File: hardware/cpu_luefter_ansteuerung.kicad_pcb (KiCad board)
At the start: 2 copper layers, 26 parts, among them IC1 ATMEGA8A-A, P1 POWER 12V DC, P2 ISP, P3 CPU LUEFTER, Q1 BC817-40, SW1 SW_PUSH, U1 7805, U2 CD4543, Y1 Crystal 12MHz

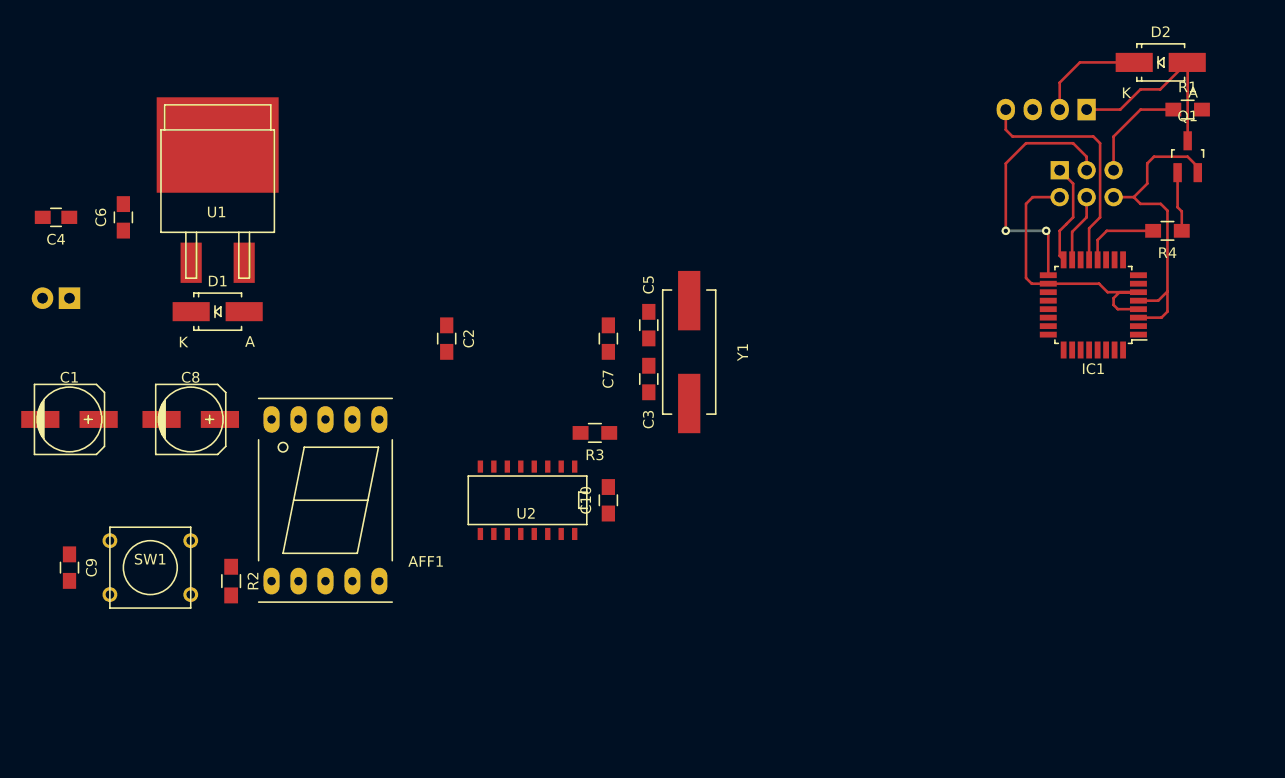
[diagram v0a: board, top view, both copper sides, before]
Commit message: Portierung zu KiCad 5.1.2
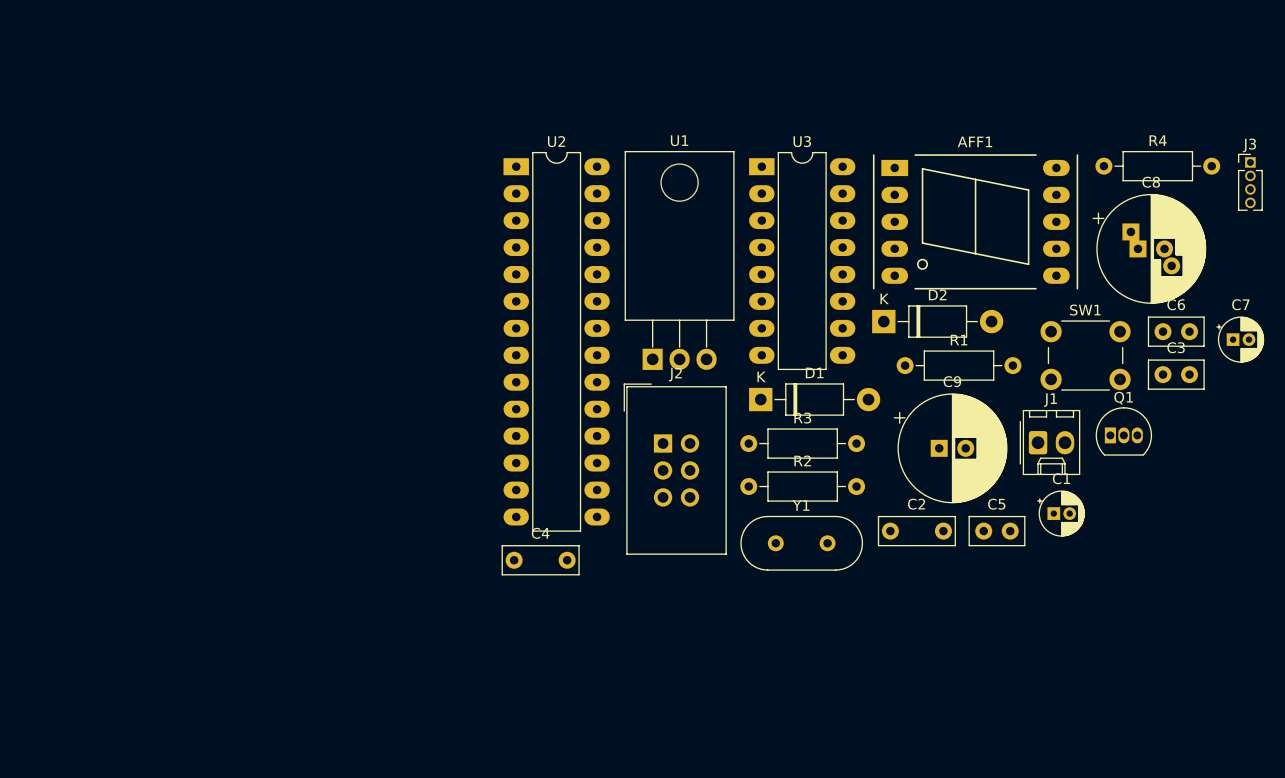
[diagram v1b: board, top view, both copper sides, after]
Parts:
- removed C10: 100n, Capacitors_SMD:C_0805_HandSoldering
- removed IC1: ATMEGA8A-A, Housings_QFP:TQFP-32_7x7mm_Pitch0.8mm
- removed P1: POWER 12V DC, Pin_Headers:Pin_Header_Straight_1x02
- removed P2: ISP, Pin_Headers:Pin_Header_Straight_2x03
- removed P3: CPU LUEFTER, Pin_Headers:Pin_Header_Straight_1x04
- added J1: Power 12V DC, Connector_Molex:Molex_KK-254_AE-6410-02A_1x02_P2.54mm_Vertical, F.Cu at (172.6, 110.1)
- added J2: ISP, Connector_IDC:IDC-Header_2x03_P2.54mm_Vertical, F.Cu at (137.2, 110.2)
- added J3: CPU Lüfter, Connector_PinHeader_1.27mm:PinHeader_1x04_P1.27mm_Vertical, F.Cu at (192.6, 83.7)
- added U3: 4543, Package_DIP:DIP-16_W7.62mm_LongPads, F.Cu at (146.5, 84.1)
- AFF1: value 7SEGMENTS LTS-5811R -> 7SEGMENTS; footprint Displays_7-Segment:7SegmentLED_LTS6760_LTS6780 -> Display_7Segment:7SegmentLED_LTS6760_LTS6780
- C1: footprint Capacitors_SMD:c_elec_6.3x5.7 -> Capacitor_THT:CP_Radial_D4.0mm_P1.50mm
- C2, C4: value 100n -> 22p; footprint Capacitors_SMD:C_0805_HandSoldering -> Capacitor_THT:C_Disc_D7.0mm_W2.5mm_P5.00mm
- C3, C5: value 22p -> 100n; footprint Capacitors_SMD:C_0805_HandSoldering -> Capacitor_THT:C_Disc_D5.0mm_W2.5mm_P2.50mm
- C6: footprint Capacitors_SMD:C_0805_HandSoldering -> Capacitor_THT:C_Disc_D5.0mm_W2.5mm_P2.50mm
- C7: value 100n -> 100u; footprint Capacitors_SMD:C_0805_HandSoldering -> Capacitor_THT:CP_Radial_D4.0mm_P1.50mm
- C8: value 100u -> 1u; footprint Capacitors_SMD:c_elec_6.3x5.7 -> Capacitor_THT:CP_Radial_D10.0mm_P2.50mm_P5.00mm
- C9: value 1u -> 100n; footprint Capacitors_SMD:C_0805_HandSoldering -> Capacitor_THT:CP_Radial_D10.0mm_P2.50mm
- D1, D2: footprint Diodes_SMD:SMA_Handsoldering -> Diode_THT:D_DO-41_SOD81_P10.16mm_Horizontal
- Q1: value BC817-40 -> BC337; footprint TO_SOT_Packages_SMD:SOT-23_Handsoldering -> Package_TO_SOT_THT:TO-92_Inline
- R1, R2, R3, R4: footprint Resistors_SMD:R_0805_HandSoldering -> Resistor_THT:R_Axial_DIN0207_L6.3mm_D2.5mm_P10.16mm_Horizontal
- SW1: value SW_PUSH -> SW_Push; footprint Buttons_Switches_ThroughHole:SW_PUSH_SMALL -> Button_Switch_THT:SW_PUSH_6mm_H5mm
- U1: footprint TO_SOT_Packages_SMD:SOT-404 -> Package_TO_SOT_THT:TO-220-3_Horizontal_TabDown
- U2: value CD4543 -> ATmega8-16PU; footprint SMD_Packages:SO-16-N -> Package_DIP:DIP-28_W7.62mm_LongPads
- Y1: footprint Crystals:Crystal_HC49-SD_SMD -> Crystal:Crystal_HC49-4H_Vertical
- moved C6 98.6 mm to (184.4, 99.7), turned to 0 degrees
- moved C1 93.2 mm to (174.1, 116.8)
- moved C8 90.7 mm to (182.0, 91.9)
- moved SW1 87.8 mm to (173.8, 99.7)
- moved C9 82.8 mm to (163.3, 110.7), turned to 0 degrees
- moved AFF1 62.1 mm to (159.1, 84.2), turned to 0 degrees
- moved C7 58.9 mm to (191.0, 100.4), turned to 0 degrees
- moved C4 53.9 mm to (123.2, 121.2), turned to 0 degrees
- moved D1 51.9 mm to (146.4, 106.1)
- moved R2 49.6 mm to (145.3, 114.3), turned to 0 degrees
- moved C3 48.5 mm to (184.4, 103.7), turned to 0 degrees
- moved C2 45.6 mm to (158.7, 118.5), turned to 0 degrees
- moved U1 43.5 mm to (136.3, 102.3)
- moved C5 37.1 mm to (167.5, 118.5), turned to 0 degrees
- moved R1 35.9 mm to (160.1, 102.9)
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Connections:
- AFF1 pad 1: Net-(AFF1-Pad1) -> +5V
- AFF1 pad 5: +5V -> Net-(AFF1-Pad5)
- C2 pad 1: +5V -> GND
- C2 pad 2: GND -> Net-(C2-Pad2)
- C3 pad 1: Net-(C3-Pad1) -> +12V
- C4 pad 1: +12V -> GND
- C4 pad 2: GND -> Net-(C4-Pad2)
- C5 pad 1: Net-(C5-Pad1) -> +5V
- C8 pad 1: +5V -> Net-(C8-Pad1)
- C9 pad 1: GND -> +5V
- C9 pad 2: Net-(C9-Pad2) -> GND
- Q1 pad 1: Net-(Q1-Pad1) -> Net-(D2-Pad2)
- Q1 pad 2: GND -> Net-(Q1-Pad2)
- Q1 pad 3: Net-(D2-Pad2) -> GND
- R1 pad 1: Net-(IC1-Pad29) -> Net-(J2-Pad5)
- R2 pad 1: +5V -> Net-(C8-Pad1)
- R2 pad 2: Net-(C9-Pad2) -> +5V
- R3 pad 1: +5V -> Net-(R3-Pad1)
- R3 pad 2: Net-(R3-Pad2) -> +5V
- R4 pad 1: Net-(Q1-Pad1) -> Net-(Q1-Pad2)
- R4 pad 2: Net-(IC1-Pad12) -> Net-(R4-Pad2)
- SW1 pad 1: Net-(C9-Pad2) -> Net-(C8-Pad1)
- U1 pad 1: +12V -> +5V
- U1 pad 3: +5V -> +12V
- U2 pad 1: Net-(R3-Pad2) -> Net-(J2-Pad5)
- U2 pad 10: Net-(AFF1-Pad7) -> Net-(C4-Pad2)
- U2 pad 11: Net-(AFF1-Pad3) -> Net-(U2-Pad11)
- U2 pad 12: Net-(AFF1-Pad2) -> Net-(U2-Pad12)
- U2 pad 13: Net-(AFF1-Pad1) -> Net-(U2-Pad13)
- U2 pad 14: Net-(AFF1-Pad9) -> Net-(R4-Pad2)
- U2 pad 15: Net-(AFF1-Pad10) -> Net-(J3-Pad4)
- U2 pad 16: +5V -> Net-(U2-Pad16)
- U2 pad 6: Net-(R3-Pad2) -> Net-(U2-Pad6)
- U2 pad 7: GND -> +5V
- U2 pad 9: Net-(AFF1-Pad8) -> Net-(C2-Pad2)
- Y1 pad 1: Net-(C5-Pad1) -> Net-(C2-Pad2)
- Y1 pad 2: Net-(C3-Pad1) -> Net-(C4-Pad2)
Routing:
- net GND: track 30.9 -> 0.00 mm
- net +5V: track 27.3 -> 0.00 mm
- net Net-(IC1-Pad17): track 24.6 -> 0.00 mm, vias 2 -> 0
- net Net-(IC1-Pad13): track 22.7 -> 0.00 mm
- net Net-(D2-Pad2): track 18.7 -> 0.00 mm
- net +12V: track 10.4 -> 0.00 mm
- net Net-(IC1-Pad29): track 9.86 -> 0.00 mm
- net Net-(IC1-Pad16): track 9.66 -> 0.00 mm
- net Net-(IC1-Pad12): track 7.46 -> 0.00 mm
- net Net-(IC1-Pad15): track 7.11 -> 0.00 mm
- net Net-(Q1-Pad1): track 5.65 -> 0.00 mm

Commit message: pcb angefangen, Bauteile schon mal angeordnet.
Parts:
- removed AFF1: 7SEGMENTS, Display_7Segment:7SegmentLED_LTS6760_LTS6780
- removed C5, C6: 100n, Capacitor_THT:C_Disc_D5.0mm_W2.5mm_P2.50mm
- removed C7: 100u, Capacitor_THT:CP_Radial_D4.0mm_P1.50mm
- removed C8: 1u, Capacitor_THT:CP_Radial_D10.0mm_P2.50mm_P5.00mm
- removed C9: 100n, Capacitor_THT:CP_Radial_D10.0mm_P2.50mm
- removed D2: 1N4001, Diode_THT:D_DO-41_SOD81_P10.16mm_Horizontal
- removed R1: 10k, Resistor_THT:R_Axial_DIN0207_L6.3mm_D2.5mm_P10.16mm_Horizontal
- removed Y1: Crystal 12MHz, Crystal:Crystal_HC49-4H_Vertical
- added R10: 560, Resistor_THT:R_Axial_DIN0207_L6.3mm_D2.5mm_P10.16mm_Horizontal, F.Cu at (134.0, 113.0)
- added R11: 560, Resistor_THT:R_Axial_DIN0207_L6.3mm_D2.5mm_P10.16mm_Horizontal, F.Cu at (121.3, 125.7)
- added R5: 560, Resistor_THT:R_Axial_DIN0207_L6.3mm_D2.5mm_P10.16mm_Horizontal, F.Cu at (134.0, 125.7)
- added R6: 560, Resistor_THT:R_Axial_DIN0207_L6.3mm_D2.5mm_P10.16mm_Horizontal, F.Cu at (121.3, 121.9)
- added R7: 560, Resistor_THT:R_Axial_DIN0207_L6.3mm_D2.5mm_P10.16mm_Horizontal, F.Cu at (121.3, 116.8)
- added R8: 560, Resistor_THT:R_Axial_DIN0207_L6.3mm_D2.5mm_P10.16mm_Horizontal, F.Cu at (121.3, 113.0)
- added R9: 560, Resistor_THT:R_Axial_DIN0207_L6.3mm_D2.5mm_P10.16mm_Horizontal, F.Cu at (134.0, 116.8)
- added REF**: MountingHole_3.2mm_M3_DIN965_Pad, MountingHole:MountingHole_3.2mm_M3_DIN965_Pad, F.Cu at (148.6, 135.9)
- added REF**: MountingHole_3.2mm_M3_DIN965_Pad, MountingHole:MountingHole_3.2mm_M3_DIN965_Pad, F.Cu at (105.4, 135.9)
- added REF**: MountingHole_3.2mm_M3_DIN965_Pad, MountingHole:MountingHole_3.2mm_M3_DIN965_Pad, F.Cu at (148.6, 76.2)
- added REF**: MountingHole_3.2mm_M3_DIN965_Pad, MountingHole:MountingHole_3.2mm_M3_DIN965_Pad, F.Cu at (105.4, 76.2)
- added U4: KCSA02-123, Display_7Segment:HDSP-7801, F.Cu at (125.1, 114.3)
- C1: value 100u -> 100n; footprint Capacitor_THT:CP_Radial_D4.0mm_P1.50mm -> Capacitor_THT:C_Disc_D5.0mm_W2.5mm_P2.50mm
- C2: value 22p -> 100n; footprint Capacitor_THT:C_Disc_D7.0mm_W2.5mm_P5.00mm -> Capacitor_THT:C_Disc_D5.0mm_W2.5mm_P2.50mm
- C3: value 100n -> 0,33u
- C4: value 22p -> 0,1u; footprint Capacitor_THT:C_Disc_D7.0mm_W2.5mm_P5.00mm -> Capacitor_THT:C_Disc_D5.0mm_W2.5mm_P2.50mm
- R3: value 10k -> 220
- R4: value 220 -> 560
- U2: value ATmega8-16PU -> ATtiny24A-PU; footprint Package_DIP:DIP-28_W7.62mm_LongPads -> Package_DIP:DIP-14_W7.62mm
- U3: value 4543 -> 74HC595
- moved C3 70.1 mm to (114.3, 105.4), turned to 180 degrees
- moved J1 67.4 mm to (114.3, 76.2), turned to 270 degrees
- moved C1 61.4 mm to (118.1, 91.4), turned to 90 degrees
- moved SW1 58.7 mm to (124.5, 131.4)
- moved R4 58.7 mm to (134.0, 121.9)
- moved J3 52.2 mm to (141.0, 76.2)
- moved Q1 43.4 mm to (143.5, 85.1), turned to 180 degrees
- moved U3 36.3 mm to (118.1, 106.7), turned to 90 degrees
- moved J2 33.4 mm to (130.8, 77.5), turned to 270 degrees
- moved U1 28.9 mm to (107.3, 101.6)
- moved C2 23.8 mm to (139.7, 104.1), turned to 90 degrees
- moved D1 23.5 mm to (147.3, 82.5), turned to 270 degrees
- moved C4 23.3 mm to (106.0, 105.4)
- moved R3 20.8 mm to (142.9, 89.5), turned to 270 degrees
- moved U2 9.96 mm to (121.9, 94.0), turned to 90 degrees
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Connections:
- C1 pad 1: +12V -> +5V
- C2 pad 1: GND -> +5V
- C2 pad 2: Net-(C2-Pad2) -> GND
- C4 pad 1: GND -> +5V
- C4 pad 2: Net-(C4-Pad2) -> GND
- D1 pad 2: +5V -> Net-(D1-Pad2)
- J2 pad 1: Net-(J2-Pad1) -> MISO
- J2 pad 3: Net-(J2-Pad3) -> SCK
- J2 pad 4: Net-(J2-Pad4) -> MOSI
- J2 pad 5: Net-(J2-Pad5) -> RESET
- J3 pad 1: Net-(D2-Pad2) -> Net-(D1-Pad2)
- J3 pad 4: Net-(J3-Pad4) -> FAN_PWM
- Q1 pad 1: Net-(D2-Pad2) -> Net-(D1-Pad2)
- R2 pad 1: Net-(C8-Pad1) -> +5V
- R2 pad 2: +5V -> RESET
- R3 pad 1: Net-(R3-Pad1) -> Net-(Q1-Pad2)
- R3 pad 2: +5V -> FAN_POWER
- R4 pad 1: Net-(Q1-Pad2) -> Net-(R4-Pad1)
- SW1 pad 1: Net-(C8-Pad1) -> PUSH_BUTTON1
- U2 pad 1: Net-(J2-Pad5) -> +5V
- U2 pad 10: Net-(C4-Pad2) -> Net-(U2-Pad10)
- U2 pad 11: Net-(U2-Pad11) -> 7_SEG_RCLK
- U2 pad 12: Net-(U2-Pad12) -> 7_SEG_SRCLK
- U2 pad 13: Net-(U2-Pad13) -> 7_SEG_SER
- U2 pad 14: Net-(R4-Pad2) -> GND
- U2 pad 2: Net-(U2-Pad2) -> PUSH_BUTTON1
- U2 pad 3: Net-(U2-Pad3) -> FAN_POWER
- U2 pad 4: Net-(U2-Pad4) -> RESET
- U2 pad 5: Net-(U2-Pad5) -> FAN_PWM
- U2 pad 7: +5V -> MOSI
- U2 pad 8: GND -> MISO
- U2 pad 9: Net-(C2-Pad2) -> SCK
- U3 pad 1: Net-(R3-Pad1) -> Net-(R5-Pad2)
- U3 pad 10: Net-(AFF1-Pad9) -> +5V
- U3 pad 11: Net-(AFF1-Pad8) -> 7_SEG_SRCLK
- U3 pad 12: Net-(AFF1-Pad5) -> 7_SEG_RCLK
- U3 pad 13: Net-(AFF1-Pad4) -> GND
- U3 pad 14: Net-(AFF1-Pad3) -> 7_SEG_SER
- U3 pad 15: Net-(AFF1-Pad2) -> Net-(R4-Pad2)
- U3 pad 2: Net-(U2-Pad25) -> Net-(R6-Pad2)
- U3 pad 3: Net-(U2-Pad24) -> Net-(R7-Pad2)
- U3 pad 4: Net-(U2-Pad26) -> Net-(R8-Pad2)
- U3 pad 5: Net-(U2-Pad23) -> Net-(R9-Pad2)
- U3 pad 6: Net-(R3-Pad1) -> Net-(R10-Pad2)
- U3 pad 7: GND -> Net-(R11-Pad2)
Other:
- board outline added: 50.8 x 67.3 mm

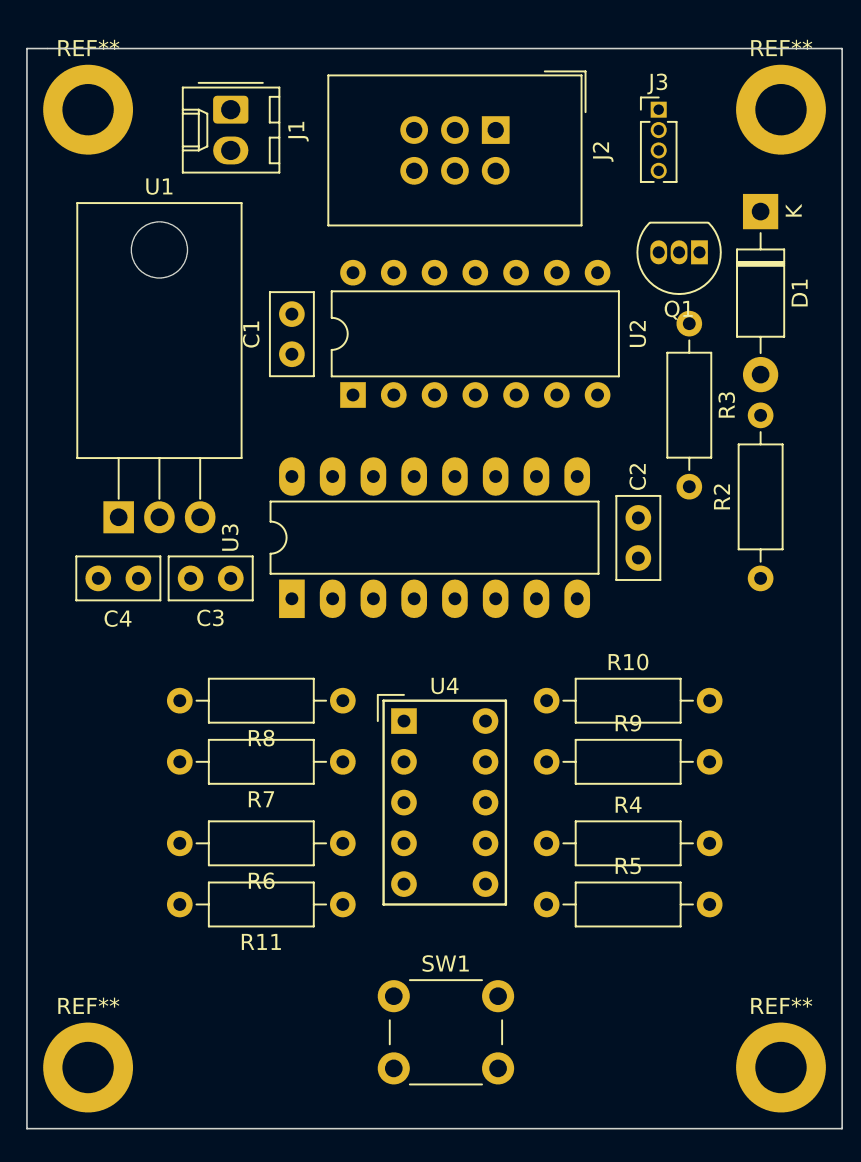
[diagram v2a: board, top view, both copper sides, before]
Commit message: PCB Hand geroutet.
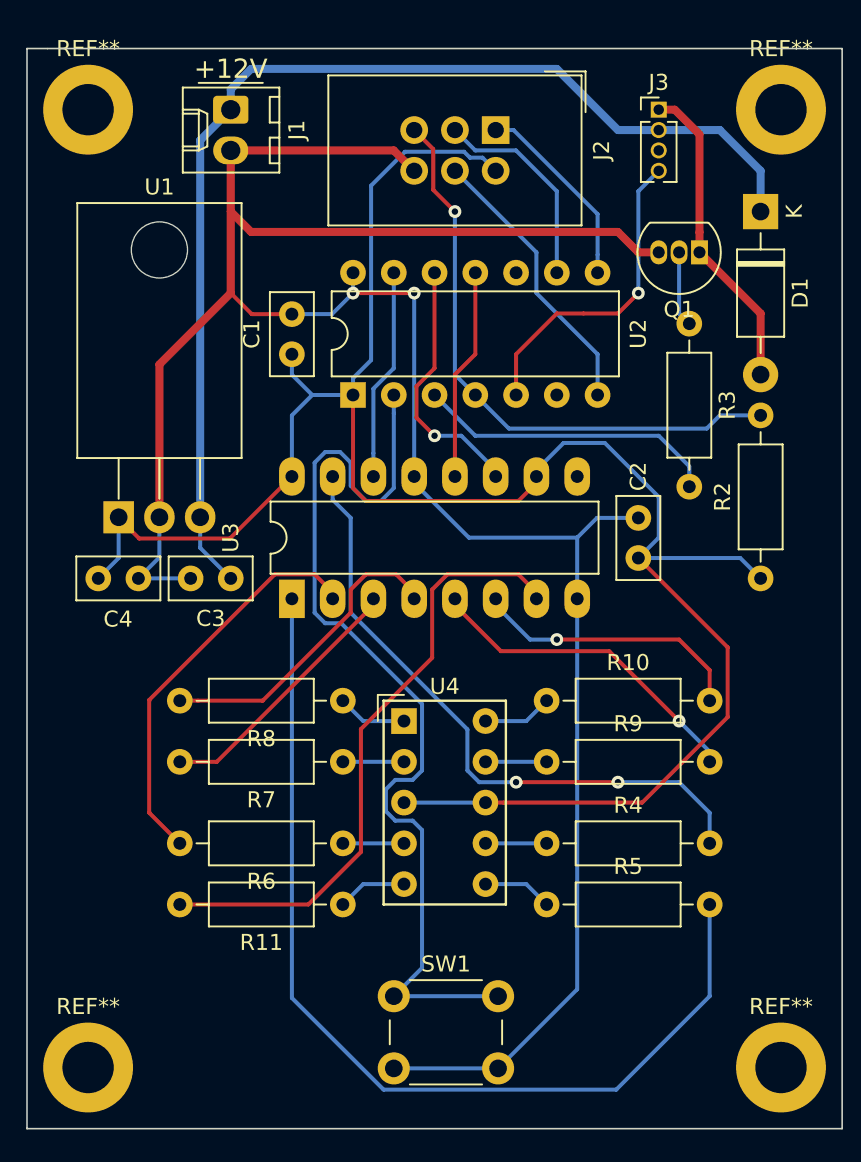
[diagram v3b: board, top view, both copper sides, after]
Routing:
- net GND: track 0.00 -> 155.1 mm, vias 0 -> 2
- net +5V: track 0.00 -> 126.8 mm
- net +12V: track 0.00 -> 70.8 mm
- net Net-(R5-Pad2): track 0.00 -> 61.4 mm
- net PUSH_BUTTON1: track 0.00 -> 60.4 mm
- net Net-(R4-Pad2): track 0.00 -> 39.9 mm, vias 0 -> 2
- net Net-(R11-Pad2): track 0.00 -> 38.6 mm
- net RESET: track 0.00 -> 37.1 mm, vias 0 -> 1
- net Net-(R6-Pad2): track 0.00 -> 25.3 mm
- net Net-(R9-Pad2): track 0.00 -> 20.7 mm, vias 0 -> 1
- net FAN_PWM: track 0.00 -> 19.9 mm, vias 0 -> 1
- net Net-(D1-Pad2): track 0.00 -> 19.7 mm
- net Net-(R8-Pad2): track 0.00 -> 19.6 mm
- net FAN_POWER: track 0.00 -> 19.0 mm
- net MOSI: track 0.00 -> 17.7 mm
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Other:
- net class +12V added: clearance 0.2, trace_width 0.5, via_dia 0.8, via_drill 0.4
- board text added: "+12V"
